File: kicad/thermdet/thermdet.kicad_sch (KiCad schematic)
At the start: 16 parts, among them J1 USB C Receptacle, SW1 SW_Reed_SPDT, SW2 SW_SPDT

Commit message: WIP
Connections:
- new net: U1. (Vhi), U3. (PwrB)
- new net: J1. (V), U1. (Vhi), U3. (PwrB)
- new net: U1. (Vhi), U2. (Vin) (x3)
- new net: U2. (Vin), U4. (Vin)
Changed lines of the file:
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@@
+	(wire
+		(pts
+			(xy 137.16 116.84) (xy 144.78 116.84)
+		)
+		(stroke
+			(width 0)
+			(type default)
+		)
+	)
 	(wire
 		(pts
@@
 	(wire
 		(pts
-			(xy 137.16 91.44) (xy 137.16 119.38)
-		)
-		(stroke
-			(width 0)
-			(type default)
-		)
-	)
-	(wire
-		(pts
 			(xy 106.68 88.9) (xy 106.68 80.01)
 		)
@@
 	(wire
 		(pts
+			(xy 137.16 91.44) (xy 137.16 116.84)
+		)
+		(stroke
+			(width 0)
+			(type default)
+		)
+	)
+	(wire
+		(pts
 			(xy 154.94 81.28) (xy 149.86 81.28)
 		)
@@
 	(wire
 		(pts
-			(xy 130.81 93.98) (xy 135.89 93.98)
-		)
-		(stroke
-			(width 0)
-			(type default)
-		)
-	)
-	(wire
-		(pts
 			(xy 74.93 80.01) (xy 77.47 80.01)
 		)
@@
 	(wire
 		(pts
-			(xy 144.78 96.52) (xy 144.78 114.3)
-		)
-		(stroke
-			(width 0)
-			(type default)
-		)
-	)
-	(wire
-		(pts
 			(xy 191.77 66.04) (xy 191.77 68.58)
 		)
@@
 	(wire
 		(pts
-			(xy 130.81 101.6) (xy 130.81 118.11)
-		)
-		(stroke
-			(width 0)
-			(type default)
-		)
-	)
-	(wire
-		(pts
 			(xy 130.81 78.74) (xy 151.13 78.74)
 		)
@@
 	(wire
 		(pts
-			(xy 138.43 121.92) (xy 144.78 121.92)
-		)
-		(stroke
-			(width 0)
-			(type default)
-		)
-	)
-	(wire
-		(pts
-			(xy 130.81 99.06) (xy 134.62 99.06)
-		)
-		(stroke
-			(width 0)
-			(type default)
-		)
-	)
-	(wire
-		(pts
 			(xy 175.26 77.47) (xy 175.26 66.04)
 		)
@@
 	(wire
 		(pts
-			(xy 137.16 119.38) (xy 144.78 119.38)
-		)
-		(stroke
-			(width 0)
-			(type default)
-		)
-	)
-	(wire
-		(pts
 			(xy 74.93 68.58) (xy 77.47 68.58)
 		)
@@
 	(wire
 		(pts
-			(xy 130.81 88.9) (xy 138.43 88.9)
-		)
-		(stroke
-			(width 0)
-			(type default)
-		)
-	)
-	(wire
-		(pts
 			(xy 130.81 83.82) (xy 143.51 83.82)
 		)
@@
 	(wire
 		(pts
+			(xy 139.7 119.38) (xy 144.78 119.38)
+		)
+		(stroke
+			(width 0)
+			(type default)
+		)
+	)
+	(wire
+		(pts
 			(xy 130.81 118.11) (xy 104.14 118.11)
 		)
@@
 	(wire
 		(pts
+			(xy 130.81 93.98) (xy 134.62 93.98)
+		)
+		(stroke
+			(width 0)
+			(type default)
+		)
+	)
+	(wire
+		(pts
 			(xy 143.51 83.82) (xy 143.51 88.9)
 		)
@@
 	(wire
 		(pts
-			(xy 135.89 93.98) (xy 135.89 116.84)
-		)
-		(stroke
-			(width 0)
-			(type default)
-		)
-	)
-	(wire
-		(pts
 			(xy 171.45 127) (xy 166.37 127)
 		)
@@
 	(wire
 		(pts
+			(xy 115.57 83.82) (xy 111.76 83.82)
+		)
+		(stroke
+			(width 0)
+			(type default)
+		)
+	)
+	(wire
+		(pts
+			(xy 74.93 57.15) (xy 77.47 57.15)
+		)
+		(stroke
+			(width 0)
+			(type default)
+		)
+	)
+	(wire
+		(pts
+			(xy 134.62 93.98) (xy 134.62 114.3)
+		)
+		(stroke
+			(width 0)
+			(type default)
+		)
+	)
+	(wire
+		(pts
+			(xy 160.02 114.3) (xy 162.56 114.3)
+		)
+		(stroke
+			(width 0)
+			(type default)
+		)
+	)
+	(wire
+		(pts
+			(xy 130.81 96.52) (xy 130.81 118.11)
+		)
+		(stroke
+			(width 0)
+			(type default)
+		)
+	)
+	(wire
+		(pts
+			(xy 187.96 121.92) (xy 193.04 121.92)
+		)
+		(stroke
+			(width 0)
+			(type default)
+		)
+	)
+	(wire
+		(pts
+			(xy 115.57 86.36) (xy 109.22 86.36)
+		)
+		(stroke
+			(width 0)
+			(type default)
+		)
+	)
+	(wire
+		(pts
+			(xy 168.91 71.12) (xy 161.29 71.12)
+		)
+		(stroke
+			(width 0)
+			(type default)
+		)
+	)
+	(wire
+		(pts
+			(xy 111.76 57.15) (xy 101.6 57.15)
+		)
+		(stroke
+			(width 0)
+			(type default)
+		)
+	)
+	(wire
+		(pts
+			(xy 134.62 114.3) (xy 144.78 114.3)
+		)
+		(stroke
+			(width 0)
+			(type default)
+		)
+	)
+	(wire
+		(pts
+			(xy 130.81 88.9) (xy 139.7 88.9)
+		)
+		(stroke
+			(width 0)
+			(type default)
+		)
+	)
+	(wire
+		(pts
+			(xy 149.86 81.28) (xy 149.86 86.36)
+		)
+		(stroke
+			(width 0)
+			(type default)
+		)
+	)
+	(wire
+		(pts
 			(xy 130.81 91.44) (xy 137.16 91.44)
 		)
@@
 	(wire
 		(pts
-			(xy 115.57 83.82) (xy 111.76 83.82)
-		)
-		(stroke
-			(width 0)
-			(type default)
-		)
-	)
-	(wire
-		(pts
-			(xy 74.93 57.15) (xy 77.47 57.15)
-		)
-		(stroke
-			(width 0)
-			(type default)
-		)
-	)
-	(wire
-		(pts
-			(xy 160.02 114.3) (xy 162.56 114.3)
-		)
-		(stroke
-			(width 0)
-			(type default)
-		)
-	)
-	(wire
-		(pts
-			(xy 138.43 88.9) (xy 138.43 121.92)
-		)
-		(stroke
-			(width 0)
-			(type default)
-		)
-	)
-	(wire
-		(pts
-			(xy 187.96 121.92) (xy 193.04 121.92)
-		)
-		(stroke
-			(width 0)
-			(type default)
-		)
-	)
-	(wire
-		(pts
-			(xy 115.57 86.36) (xy 109.22 86.36)
-		)
-		(stroke
-			(width 0)
-			(type default)
-		)
-	)
-	(wire
-		(pts
-			(xy 168.91 71.12) (xy 161.29 71.12)
-		)
-		(stroke
-			(width 0)
-			(type default)
-		)
-	)
-	(wire
-		(pts
-			(xy 111.76 57.15) (xy 101.6 57.15)
-		)
-		(stroke
-			(width 0)
-			(type default)
-		)
-	)
-	(wire
-		(pts
-			(xy 149.86 81.28) (xy 149.86 86.36)
-		)
-		(stroke
-			(width 0)
-			(type default)
-		)
-	)
-	(wire
-		(pts
-			(xy 134.62 124.46) (xy 144.78 124.46)
-		)
-		(stroke
-			(width 0)
-			(type default)
-		)
-	)
-	(wire
-		(pts
-			(xy 134.62 99.06) (xy 134.62 124.46)
-		)
-		(stroke
-			(width 0)
-			(type default)
-		)
-	)
-	(wire
-		(pts
-			(xy 135.89 116.84) (xy 144.78 116.84)
+			(xy 139.7 88.9) (xy 139.7 119.38)
 		)
 		(stroke
@@
 		(pts
 			(xy 160.02 119.38) (xy 162.56 119.38)
-		)
-		(stroke
-			(width 0)
-			(type default)
-		)
-	)
-	(wire
-		(pts
-			(xy 130.81 96.52) (xy 144.78 96.52)
 		)
 		(stroke
@@
 		(pin ""
 		)
-		(pin ""
-		)
-		(pin ""
-		)
 		(instances
 			(project "thermdet"
@@
 		)
 		(pin ""
-		)
-		(pin ""
-		)
-		(pin ""

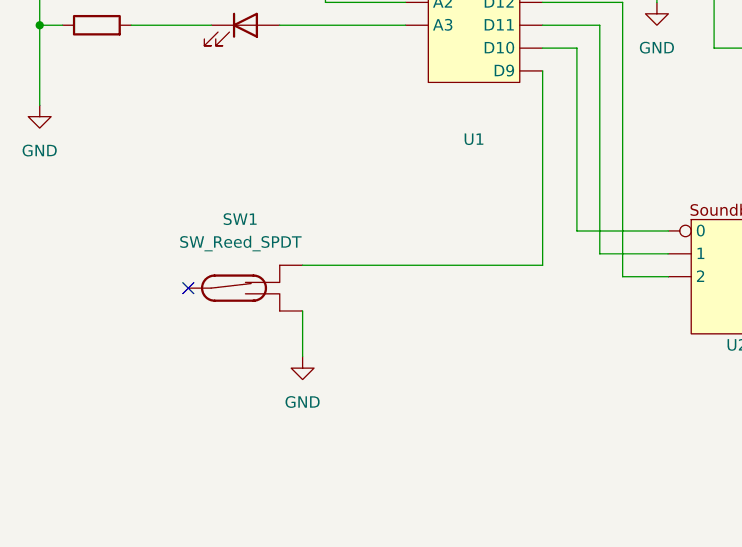
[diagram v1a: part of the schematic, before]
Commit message: Fix reed switch in schematic
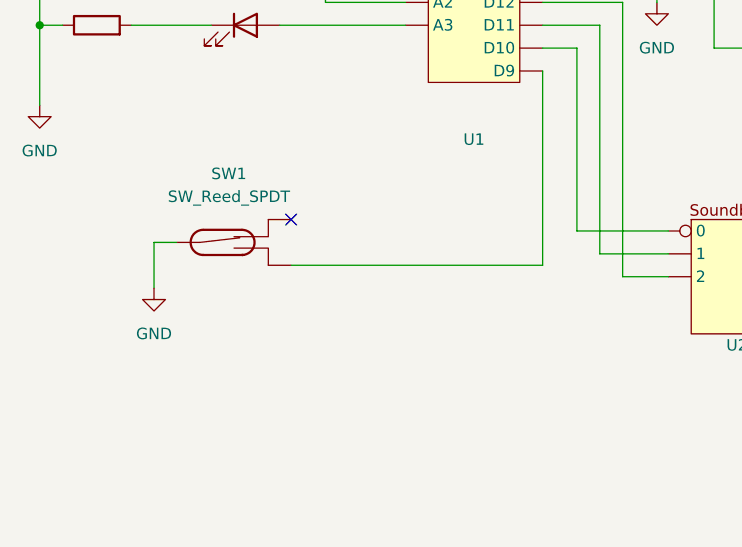
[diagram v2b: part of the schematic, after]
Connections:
- net GND: now also SW1.2; no longer SW1.3
- net at SW1.1: no longer U1. (Vhi)
- new net: U1. (Vhi), U3. (PwrB)
- new net: J1. (V), U1. (Vhi), U3. (PwrB)
- new net: U1. (Vhi), U2. (Vin) (x3)
- new net: SW1.3, U1. (Vhi)
- new net: U2. (Vin), U4. (Vin)
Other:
- moved on the sheet: SW1
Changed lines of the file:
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@@
+	)
+	(no_connect
+		(at 102.87 113.03)
 	)
 	(no_connect
 		(at 165.1 54.61)
 	)
-	(no_connect
-		(at 91.44 120.65)
-	)
 	(wire
 		(pts
@@
 	(wire
 		(pts
+			(xy 90.17 115.57) (xy 87.63 115.57)
+		)
+		(stroke
+			(width 0)
+			(type default)
+		)
+	)
+	(wire
+		(pts
 			(xy 74.93 100.33) (xy 74.93 91.44)
 		)
@@
 	(wire
 		(pts
+			(xy 102.87 118.11) (xy 130.81 118.11)
+		)
+		(stroke
+			(width 0)
+			(type default)
+		)
+	)
+	(wire
+		(pts
 			(xy 151.13 86.36) (xy 154.94 86.36)
 		)
@@
 	(wire
 		(pts
-			(xy 104.14 123.19) (xy 104.14 128.27)
-		)
-		(stroke
-			(width 0)
-			(type default)
-		)
-	)
-	(wire
-		(pts
 			(xy 74.93 91.44) (xy 74.93 80.01)
 		)
@@
 	(wire
 		(pts
-			(xy 130.81 118.11) (xy 104.14 118.11)
-		)
-		(stroke
-			(width 0)
-			(type default)
-		)
-	)
-	(wire
-		(pts
 			(xy 130.81 93.98) (xy 134.62 93.98)
 		)
@@
 		(pts
 			(xy 160.02 119.38) (xy 162.56 119.38)
+		)
+		(stroke
+			(width 0)
+			(type default)
+		)
+	)
+	(wire
+		(pts
+			(xy 87.63 115.57) (xy 87.63 120.65)
 		)
 		(stroke
@@
 	(symbol
 		(lib_id "power:GND")
-		(at 104.14 128.27 0)
+		(at 87.63 120.65 0)
 		(unit 1)
 		(exclude_from_sim no)
@@
 		(fields_autoplaced yes)
 		(property "Reference" "#PWR03"
-			(at 104.14 134.62 0)
+			(at 87.63 127 0)
 			(effects
 				(font
@@
 		)
 		(property "Value" "GND"
-			(at 104.14 133.35 0)
-			(effects
-				(font
-					(size 1.27 1.27)
-				)
-			)
-		)
-		(property "Footprint" ""
-			(at 104.14 128.27 0)
+			(at 87.63 125.73 0)
+			(effects
+				(font
+					(size 1.27 1.27)
+				)
+			)
+		)
+		(property "Footprint" ""
+			(at 87.63 120.65 0)
 			(effects
 				(font
@@
 		)
 		(property "Datasheet" ""
-			(at 104.14 128.27 0)
+			(at 87.63 120.65 0)
 			(effects
 				(font
@@
 		)
 		(property "Description" "Power symbol creates a global label with name \"GND\" , ground"
-			(at 104.14 128.27 0)
+			(at 87.63 120.65 0)
 			(effects
 				(font
@@
 	(symbol
 		(lib_id "Switch:SW_Reed_SPDT")
-		(at 96.52 120.65 0)
+		(at 95.25 115.57 0)
 		(unit 1)
 		(exclude_from_sim no)
@@
 		(fields_autoplaced yes)
 		(property "Reference" "SW1"
-			(at 97.2215 113.03 0)
+			(at 95.9515 107.95 0)
 			(effects
 				(font
@@
 		)
 		(property "Value" "SW_Reed_SPDT"
-			(at 97.2215 115.57 0)
-			(effects
-				(font
-					(size 1.27 1.27)
-				)
-			)
-		)
-		(property "Footprint" ""
-			(at 96.52 120.65 0)
+			(at 95.9515 110.49 0)
+			(effects
+				(font
+					(size 1.27 1.27)
+				)
+			)
+		)
+		(property "Footprint" ""
+			(at 95.25 115.57 0)
 			(effects
 				(font
@@
 		)
 		(property "Datasheet" "~"
-			(at 96.52 120.65 0)
+			(at 95.25 115.57 0)
 			(effects
 				(font
@@
 		)
 		(property "Description" "SPDT reed switch"
-			(at 96.52 120.65 0)
-			(effects
-				(font
+			(at 95.25 115.57 0)
+			(effects
+				(font
